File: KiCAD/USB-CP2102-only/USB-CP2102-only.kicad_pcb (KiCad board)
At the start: 2 copper layers, 48 x 29 mm, 33 parts, among them J1 5V, J10 TXD, J11 ESP_RST, J12 ESP_GPIO0, J2 V_USB, J3 3.3V, J4 GND, J5 GND, J6 GND, J7 XUNPU TYPEC-304S-ACP16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

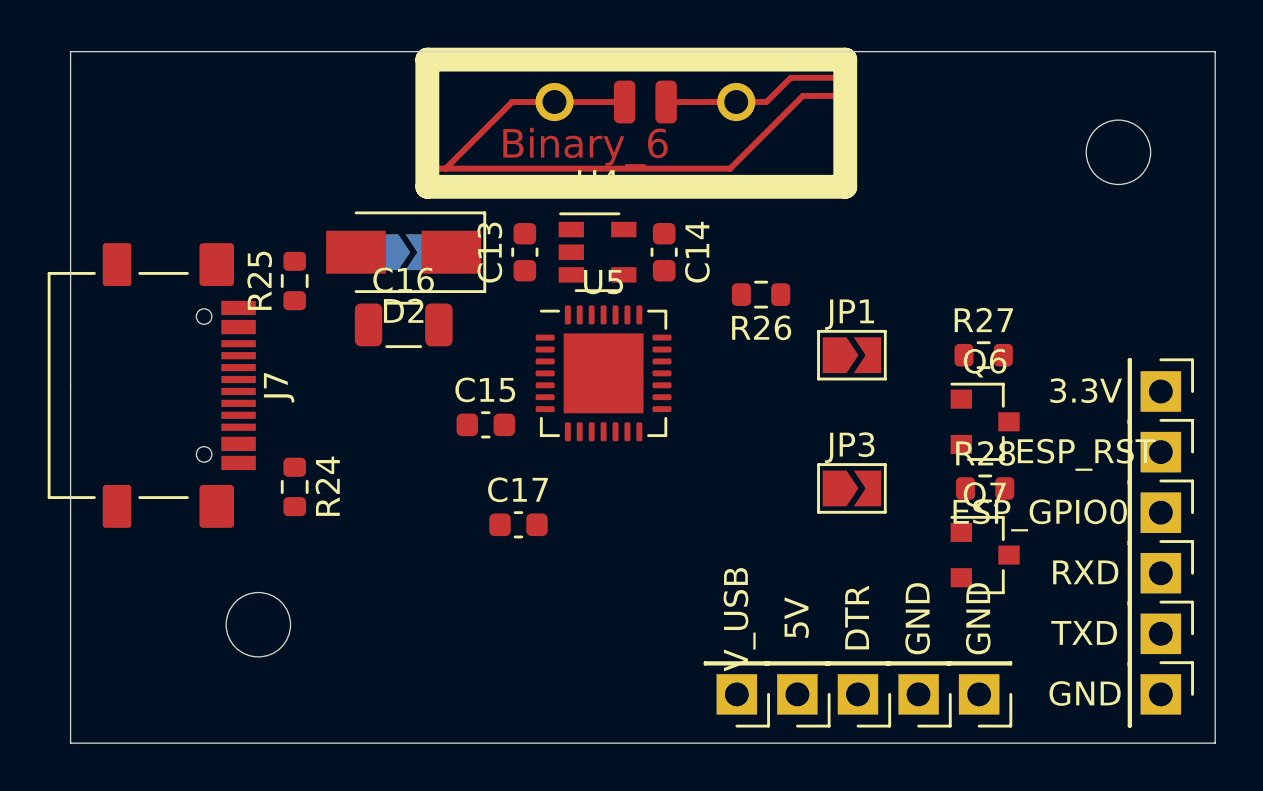
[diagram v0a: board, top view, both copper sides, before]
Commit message: Wire up initial version of PCB
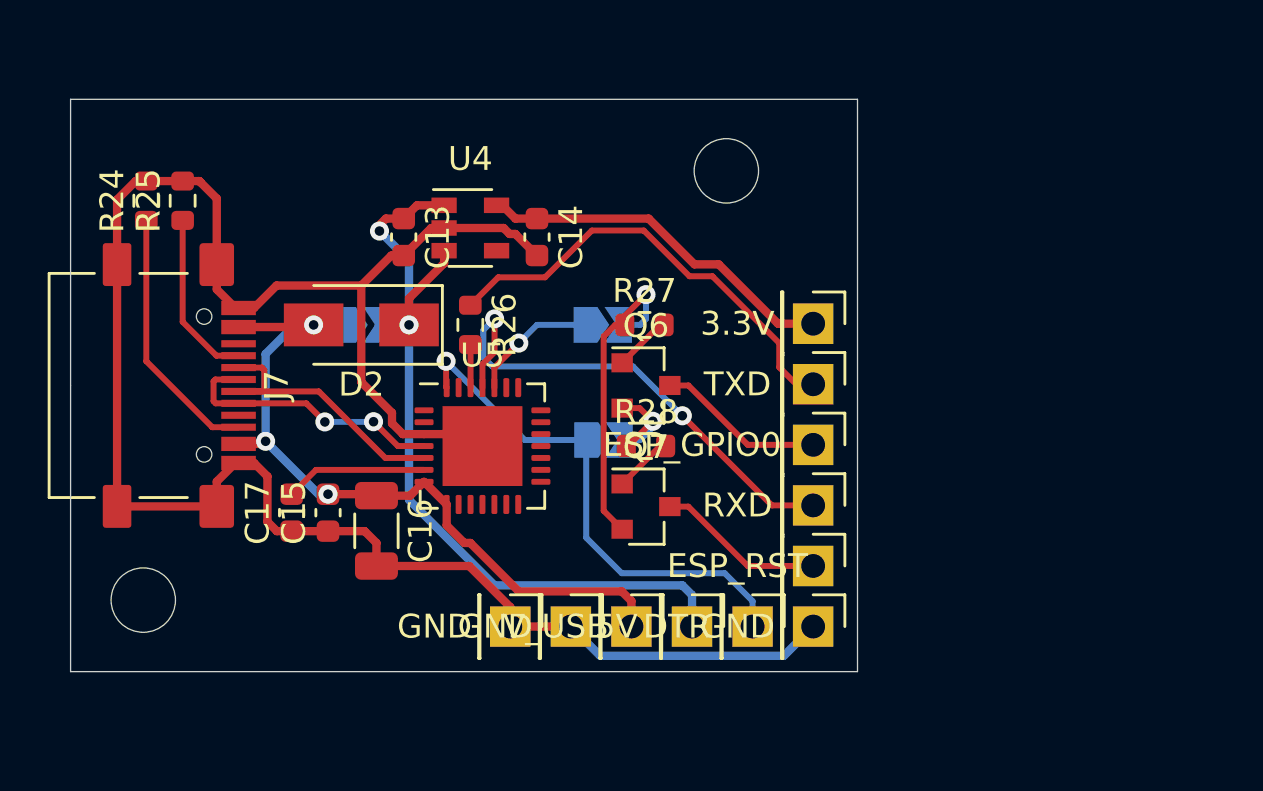
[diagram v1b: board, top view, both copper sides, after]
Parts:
- JP1, JP3: moved to B.Cu
- LOGO1: footprint MeineBib:Binary_6_v0.1 -> MeineBib:LOGO; moved to B.Cu
- moved J10 17.9 mm to (181.1, 119.9)
- moved J4 17.4 mm to (168.4, 130.1), turned to 270 degrees
- moved J5 17.4 mm to (171.0, 130.1), turned to 270 degrees
- moved HO2 16.5 mm to (177.5, 111.0)
- moved J11 15.3 mm to (181.1, 127.6)
- moved J6 14.9 mm to (181.1, 130.1)
- moved J12 14.9 mm to (181.1, 122.5)
- moved J3 14.9 mm to (181.1, 117.4)
- moved J9 14.9 mm to (181.1, 125.0)
- moved Q7 14.4 mm to (174.1, 125.1)
- moved R28 14.3 mm to (174.1, 122.5)
- moved Q6 14.3 mm to (174.1, 120.0)
- moved R27 14.3 mm to (174.1, 117.5)
- moved R24 13.5 mm to (153.2, 112.3), turned to 90 degrees
- moved R26 12.3 mm to (166.8, 117.5), turned to 270 degrees
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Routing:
- net GND: track 0.00 -> 85.0 mm
- net +5V: track 0.00 -> 34.9 mm, vias 0 -> 2
- net VBUS: track 0.00 -> 32.0 mm, vias 0 -> 3
- net DTR: track 0.00 -> 21.6 mm, vias 0 -> 1
- net GPIO1: track 0.00 -> 21.3 mm, vias 0 -> 2
- net GPIO3: track 0.00 -> 18.9 mm
- net +3V3: track 0.00 -> 15.3 mm
- net Net-(JP1-Pad2): track 0.00 -> 13.3 mm, vias 0 -> 1
- net Net-(J7-PadA7): track 0.00 -> 12.0 mm
- net Net-(J7-PadA6): track 0.00 -> 11.9 mm, vias 0 -> 2
- net Net-(J7-PadB5): track 0.00 -> 10.9 mm
- net Net-(J7-PadA5): track 0.00 -> 7.19 mm
- net RST: track 0.00 -> 7.04 mm
- net GPIO0: track 0.00 -> 7.04 mm
- net Net-(C17-Pad2): track 0.00 -> 5.97 mm
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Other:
- board size 48 x 29 mm -> 33 x 24 mm
- net class Power added: clearance 0.2, trace_width 0.35, via_dia 0.8, via_drill 0.4

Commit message: Update USB board to KiCAD 5.99
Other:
- net class Default removed
- net class Power removed

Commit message: Beautify PCB
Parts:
- added ?: , buzzardLabel, F.Cu at (179.9, 125.0)
- added ?: , buzzardLabel, F.Cu at (171.0, 128.8)
- added ?: , buzzardLabel, F.Cu at (179.9, 122.5)
- added ?: , buzzardLabel, B.Cu at (155.4, 117.5)
- added ?: , buzzardLabel, B.Cu at (168.1, 119.8)
- added ?: , buzzardLabel, B.Cu at (165.2, 117.5)
- added ?: , buzzardLabel, F.Cu at (179.9, 127.6)
- added ?: , buzzardLabel, F.Cu at (179.9, 117.4)
- added ?: , buzzardLabel, F.Cu at (173.5, 128.8)
- added ?: , buzzardLabel, F.Cu at (168.4, 128.8)
- added ?: , buzzardLabel, F.Cu at (176.1, 128.8)
- added ?: , buzzardLabel, F.Cu at (179.9, 119.9)
- added ?: , buzzardLabel, F.Cu at (165.9, 128.8)
- added ?: , buzzardLabel, F.Cu at (179.4, 130.1)
- added REF**: Symbol_Danger_CopperTop_Small, Symbol:Symbol_Danger_CopperTop_Small, F.Cu at (159.8, 112.0)
- moved J4 2.54 mm to (165.9, 130.1), turned to 180 degrees
- moved J8 2.54 mm to (176.1, 130.1), turned to 180 degrees
- moved J1 2.54 mm to (173.5, 130.1), turned to 180 degrees
- moved J2 2.54 mm to (171.0, 130.1), turned to 180 degrees
- moved J5 2.54 mm to (168.4, 130.1), turned to 180 degrees
- moved LOGO1 0.71 mm to (163.2, 110.6)
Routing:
- net +5V: track 34.9 -> 32.2 mm
- net DTR: track 21.6 -> 19.1 mm
- added copper zone on B.Cu, net GND
- added copper zone on F.Cu, net GND
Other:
- board text added: "Testboard USB-C + CP2102 Chrismettal 2021"

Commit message: Create initial gerbers and BOM for USB testo
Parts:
- moved LOGO1 3.10 mm to (166.3, 110.5)
- moved HO2 2.50 mm to (180.0, 111.0)
- moved ? 1.74 mm to (179.9, 128.4), turned to 0 degrees
- moved ? 1.67 mm to (179.9, 123.4)
- moved ? 1.67 mm to (179.9, 120.8)
- moved ? 1.67 mm to (179.9, 125.9)
- moved ? 1.67 mm to (179.9, 115.7)
- moved ? 1.67 mm to (179.9, 118.3)
- moved J10 1.67 mm to (181.1, 118.3)
- moved J11 1.67 mm to (181.1, 125.9)
- moved J12 1.67 mm to (181.1, 120.8)
- moved J3 1.67 mm to (181.1, 115.7)
- moved J6 1.67 mm to (181.1, 128.4)
- moved J9 1.67 mm to (181.1, 123.4)
- turned ? to 90 degrees
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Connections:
- J7 pad A8: Net-(J7-PadA8) -> unconnected-(J7-PadA8)
- J7 pad B8: Net-(J7-PadB8) -> unconnected-(J7-PadB8)
- U4 pad 4: Net-(U4-Pad4) -> unconnected-(U4-Pad4)
- U5 pad 1: Net-(U5-Pad1) -> unconnected-(U5-Pad1)
- U5 pad 10: Net-(U5-Pad10) -> unconnected-(U5-Pad10)
- U5 pad 11: Net-(U5-Pad11) -> unconnected-(U5-Pad11)
- U5 pad 12: Net-(U5-Pad12) -> unconnected-(U5-Pad12)
- U5 pad 13: Net-(U5-Pad13) -> unconnected-(U5-Pad13)
- U5 pad 14: Net-(U5-Pad14) -> unconnected-(U5-Pad14)
- U5 pad 15: Net-(U5-Pad15) -> unconnected-(U5-Pad15)
- U5 pad 16: Net-(U5-Pad16) -> unconnected-(U5-Pad16)
- U5 pad 17: Net-(U5-Pad17) -> unconnected-(U5-Pad17)
- U5 pad 18: Net-(U5-Pad18) -> unconnected-(U5-Pad18)
- U5 pad 19: Net-(U5-Pad19) -> unconnected-(U5-Pad19)
- U5 pad 2: Net-(U5-Pad2) -> unconnected-(U5-Pad2)
- U5 pad 20: Net-(U5-Pad20) -> unconnected-(U5-Pad20)
- U5 pad 21: Net-(U5-Pad21) -> unconnected-(U5-Pad21)
- U5 pad 22: Net-(U5-Pad22) -> unconnected-(U5-Pad22)
- U5 pad 23: Net-(U5-Pad23) -> unconnected-(U5-Pad23)
- U5 pad 27: Net-(U5-Pad27) -> unconnected-(U5-Pad27)
- U5 pad 9: Net-(U5-Pad9) -> unconnected-(U5-Pad9)
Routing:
- net VBUS: track 31.9 -> 30.1 mm
- net Net-(J7-PadA7): track 12.0 -> 11.0 mm
- net +3V3: track 15.3 -> 14.4 mm
- net RST: track 7.04 -> 6.35 mm
- net GPIO0: track 7.04 -> 6.35 mm
- net GND: track 85.5 -> 85.1 mm, vias 0 -> 2
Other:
- outline, holes or cut-outs redrawn
- board text added: "Testboard USB-C + CP2102 Chrismettal 2021_02"
- board text removed: "Testboard USB-C + CP2102 Chrismettal 2021"
